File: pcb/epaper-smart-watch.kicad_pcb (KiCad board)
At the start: 4 copper layers, 29.2 x 29.2 mm, 68 parts, among them J1 AXT624124, J3 Lithium Battery 3.7V, M1 Motor_DC, P1 USB_C_Plug_USB2.0, Q1 MMBT3904, Q3 Si1308EDL, SW1 BTN, SW2 BTN, SW3 BTN, SW4 BTN, U1 CH340E, U2 STM32WB1MMCH6TR, U3 LSM6DSOWTR

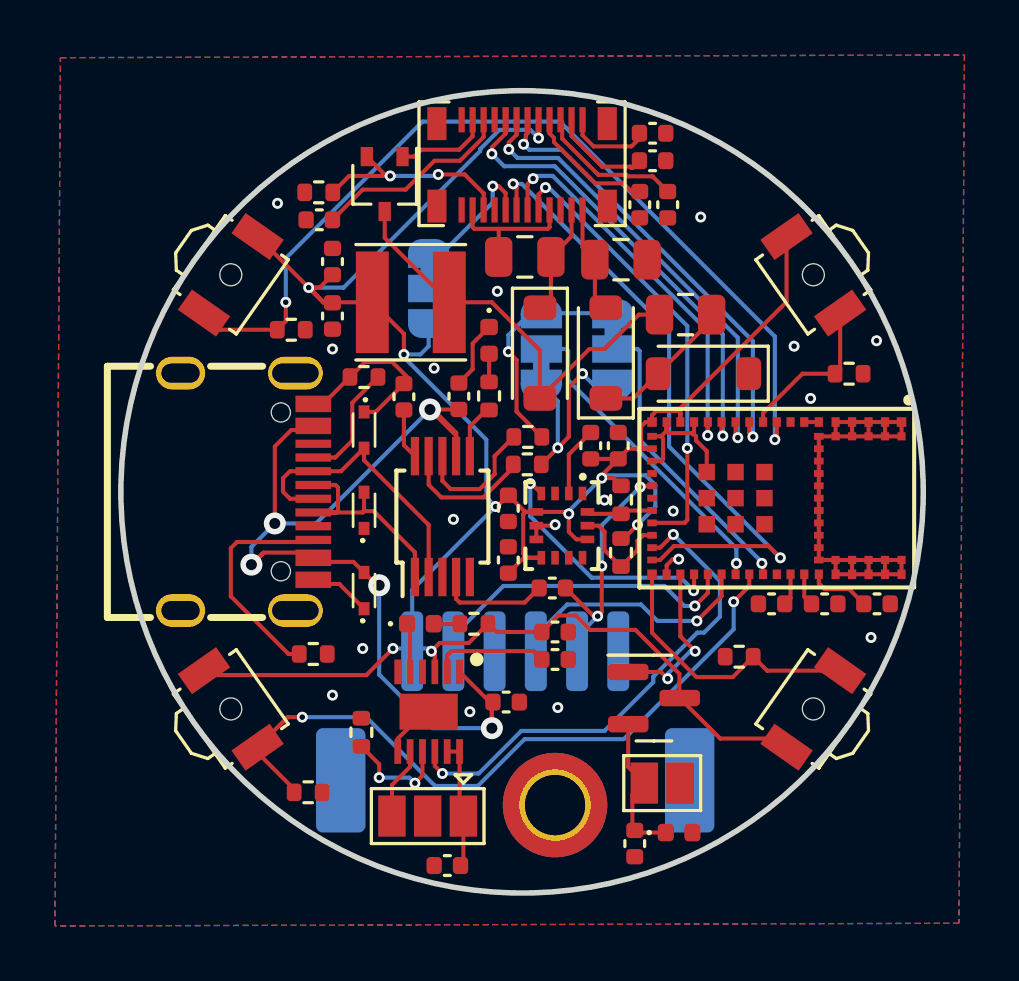
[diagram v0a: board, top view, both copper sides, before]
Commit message: Thickened power traces, fixed JP3 and removed pulldowns for buttons
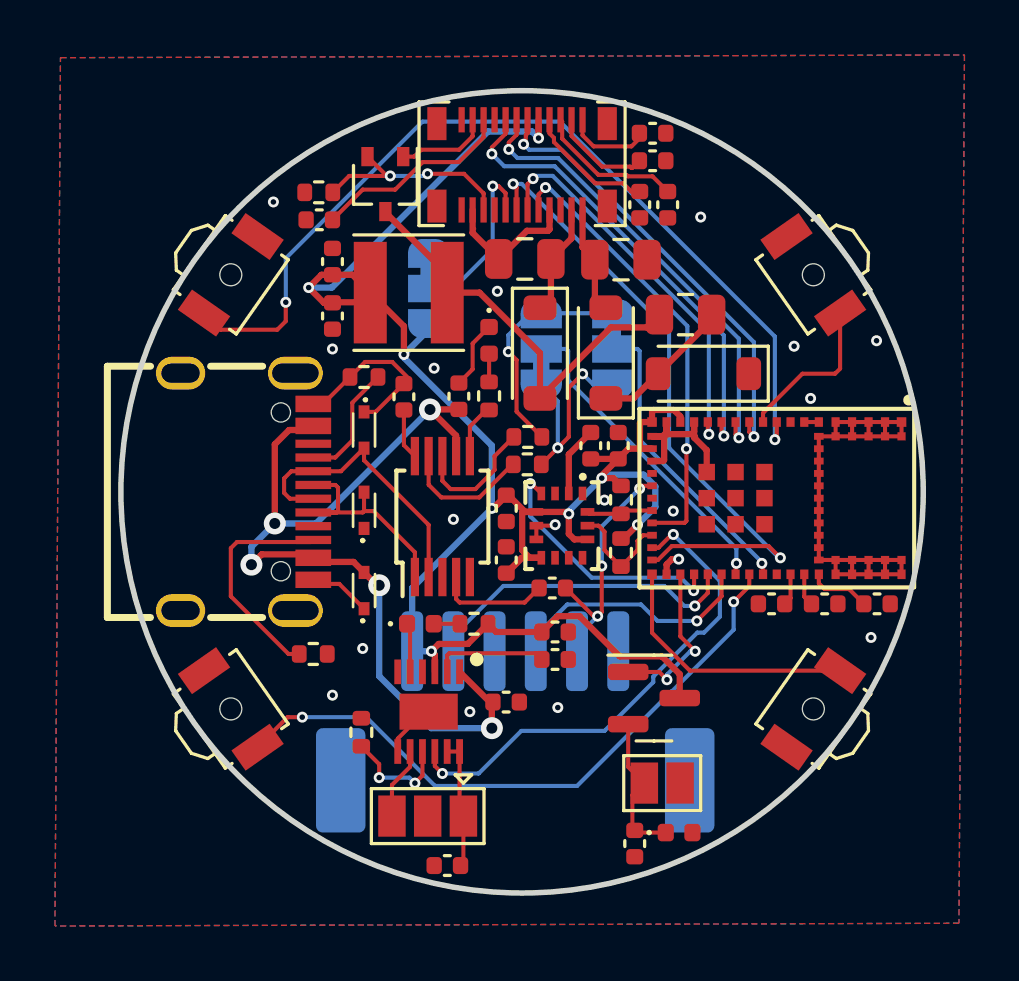
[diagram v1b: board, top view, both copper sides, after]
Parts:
- removed R1, R10, R11, R2: 10K, Resistor_SMD:R_0402_1005Metric
- removed REF**: MountingHole_2.2mm_M2_DIN965_Pad_TopBottom, MountingHole:MountingHole_2.2mm_M2_DIN965_Pad_TopBottom
- moved L1 0.36 mm to (139.7, 88.8)
- moved C24 0.08 mm to (143.2, 98.5)
- moved C25 0.08 mm to (143.2, 96.6)
- moved C3 0.08 mm to (143.9, 87.5)
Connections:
- JP3 pad 1: Net-(J1-Pin_16) -> GND
- JP3 pad 2: GND -> Net-(J1-Pin_16)
- SW1 pad 2: /EPD_VDD -> GND
- SW2 pad 1: /EPD_VDD -> GND
- SW3 pad 2: /EPD_VDD -> GND
- SW4 pad 2: /EPD_VDD -> GND
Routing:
- net /EPD_VDD: track 93.0 -> 74.2 mm, vias 9 -> 8
- net GND: track 48.8 -> 55.8 mm
- net /VBUS: track 37.4 -> 34.3 mm
- net /BTN_4: track 25.7 -> 23.6 mm
- net Net-(J1-Pin_16): track 4.87 -> 6.40 mm
- net Net-(D7-A): track 15.7 -> 14.9 mm
- net /BTN_3: track 10.2 -> 9.55 mm
- net /SWDIO: track 9.21 -> 8.65 mm
- net /SWDCLK: track 11.7 -> 11.2 mm
- net /NRST: track 8.97 -> 8.43 mm

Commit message: Use different accelerometer
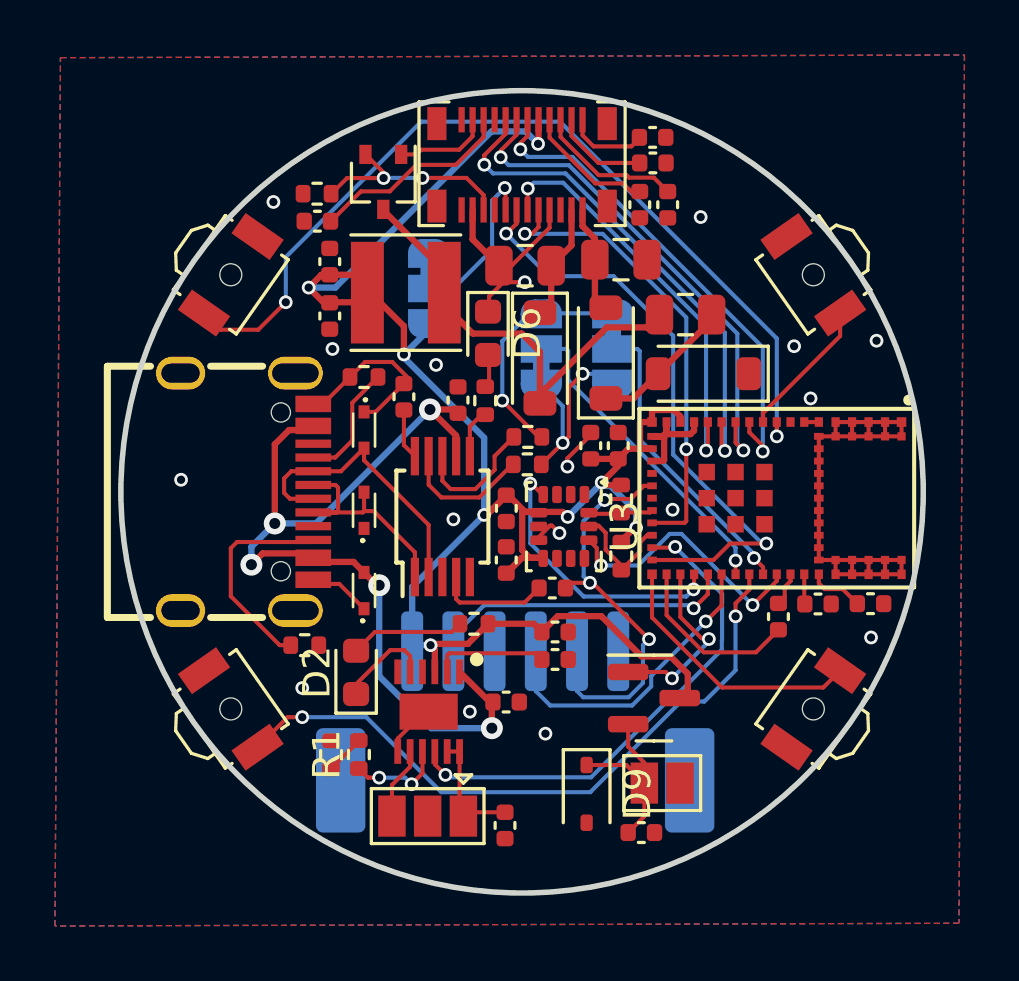
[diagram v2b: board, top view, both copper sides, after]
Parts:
- added G***: LOGO, walking-boat:Walking boat 0.5, B.Cu at (152.2, 95.9)
- added R1: 2k, Resistor_SMD:R_0402_1005Metric, F.Cu at (137.9, 105.6)
- added kibuzzard-6782824E: G***, kibuzzard-6782824E, B.Cu at (155.2, 95.6)
- D2, D6: footprint LED_SMD:LED_0402_1005Metric -> LED_SMD:LED_0603_1608Metric
- D9: footprint Diode_SMD:D_0402_1005Metric -> Diode_SMD:D_SOD-323
- R9: value 4k -> 2k
- U3: value LSM6DSOWTR -> LSM6DS3; footprint EasyEda2Kicad:LGA-14L_L3.0-W2.5-P0.50-TL -> Package_LGA:LGA-14_3x2.5mm_P0.5mm_LayoutBorder3x4y
- moved D9 3.65 mm to (146.2, 107.0), turned to -90 degrees
- moved D2 2.93 mm to (137.8, 102.6), turned to 90 degrees
- moved C12 2.56 mm to (143.2, 108.1), turned to -90 degrees
- moved R9 1.37 mm to (136.8, 105.6)
- moved C19 0.53 mm to (153.1, 100.5), turned to -90 degrees
- moved C23 0.47 mm to (148.1, 108.4), turned to 0 degrees
- moved R3 0.45 mm to (135.9, 101.6)
- moved D6 0.26 mm to (142.6, 90.2)
- moved C3 0.25 mm to (143.9, 87.8)
- moved C20 0.24 mm to (154.6, 100.1)
- moved C21 0.24 mm to (156.5, 100.1)
- moved R14 0.22 mm to (142.5, 92.7)
- moved D7 0.18 mm to (144.4, 91.1)
- moved C4 0.15 mm to (148.6, 83.1)
- moved C15 0.14 mm to (141.5, 92.7)
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- renumbered R8 to R2
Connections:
- R9 pad 1: Net-(PS1-ISET) -> Net-(R1-Pad2)
- U2 pad 39: unconnected-(U2-PA5-Pad39) -> /Accel_CS
- U3 pad 1: GND -> unconnected-(U3-SDO/SA0-Pad1)
- U3 pad 12: /EPD_VDD -> /Accel_CS
- U3 pad 2: GND -> unconnected-(U3-SDX-Pad2)
- U3 pad 3: GND -> unconnected-(U3-SCX-Pad3)
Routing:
- net /Accel_CS: track 0.00 -> 9.65 mm, vias 0 -> 2
- net /NRST: track 8.43 -> 14.9 mm
- net Net-(D2-A): track 0.95 -> 4.19 mm
- net /SWDIO: track 8.65 -> 11.3 mm
- net /EPD_VDD: track 74.2 -> 71.7 mm
- net Net-(D9-K): track 5.32 -> 7.42 mm
- net /BUSY: track 16.8 -> 18.6 mm
- net /RST_N: track 23.9 -> 22.1 mm
- net /DC: track 16.7 -> 18.4 mm
- net /EPD_SPICL: track 16.4 -> 18.1 mm
- net /CHG: track 1.64 -> 3.14 mm
- net Net-(R1-Pad2): track 0.00 -> 1.43 mm
- net /BTN_4: track 23.6 -> 24.7 mm
- net GND: track 55.8 -> 54.7 mm, vias 18 -> 17
- net /CSB: track 14.2 -> 15.1 mm
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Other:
- copper layers 4 -> 2
